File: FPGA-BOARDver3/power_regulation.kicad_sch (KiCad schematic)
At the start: 27 parts, among them Q7 DMG2305UX-13, U14 TLV62130RGTT, U15 LP5907MFX-3.3, U16 REF3012

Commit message: Power Regulation sheet 2 added
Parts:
- removed L4: 600ohm/100Mhz, symbol Device:L_Iron
- added FL2: 600Ohm/100Mhz, BLM18AG601SZ1D:BEADC1608X95N, symbol BLM18AG601SZ1D:BLM18AG601SZ1D
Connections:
- net +1V8: now also FL2.1
- net XADC1V8: now also FL2.2
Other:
- moved on the sheet: C26
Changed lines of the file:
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@@
 	)
 	(junction
+		(at 50.8 152.4)
+		(diameter 0)
+		(color 0 0 0 0)
+	)
+	(junction
 		(at 151.13 67.31)
 		(diameter 0)
@@
 	)
 	(junction
-		(at 50.8 152.4)
-		(diameter 0)
-		(color 0 0 0 0)
-	)
-	(junction
 		(at 54.61 129.54)
 		(diameter 0)
@@
 	)
 	(junction
-		(at 77.47 152.4)
+		(at 90.17 152.4)
 		(diameter 0)
 		(color 0 0 0 0)
@@
 	(wire
 		(pts
-			(xy 69.85 152.4) (xy 77.47 152.4)
-		)
-		(stroke
-			(width 0)
-			(type default)
-		)
-	)
-	(wire
-		(pts
 			(xy 116.84 39.37) (xy 119.38 39.37)
 		)
@@
 	(wire
 		(pts
-			(xy 77.47 152.4) (xy 86.36 152.4)
+			(xy 90.17 152.4) (xy 99.06 152.4)
 		)
 		(stroke
@@
 	(wire
 		(pts
+			(xy 50.8 152.4) (xy 55.88 152.4)
+		)
+		(stroke
+			(width 0)
+			(type default)
+		)
+	)
+	(wire
+		(pts
 			(xy 180.34 104.14) (xy 185.42 104.14)
 		)
@@
 	(wire
 		(pts
-			(xy 77.47 161.29) (xy 82.55 161.29)
+			(xy 90.17 161.29) (xy 95.25 161.29)
 		)
 		(stroke
@@
 	(wire
 		(pts
-			(xy 77.47 160.02) (xy 77.47 161.29)
+			(xy 90.17 160.02) (xy 90.17 161.29)
 		)
 		(stroke
@@
 	(wire
 		(pts
-			(xy 50.8 152.4) (xy 62.23 152.4)
-		)
-		(stroke
-			(width 0)
-			(type default)
-		)
-	)
-	(wire
-		(pts
 			(xy 168.91 35.56) (xy 170.18 35.56)
 		)
@@
 		)
 	)
+	(wire
+		(pts
+			(xy 83.82 152.4) (xy 90.17 152.4)
+		)
+		(stroke
+			(width 0)
+			(type default)
+		)
+	)
 	(global_label "REG5V0"
 		(shape input)
@@
 	(global_label "XADCGND"
 		(shape input)
-		(at 82.55 161.29 0)
+		(at 95.25 161.29 0)
 		(fields_autoplaced yes)
 		(effects
@@
 		)
 		(property "Intersheetrefs" "${INTERSHEET_REFS}"
-			(at 94.2438 161.29 0)
+			(at 106.9438 161.29 0)
 			(effects
 				(font
@@
 	(global_label "XADC1V8"
 		(shape input)
-		(at 86.36 152.4 0)
+		(at 99.06 152.4 0)
 		(fields_autoplaced yes)
 		(effects
@@
 		)
 		(property "Intersheetrefs" "${INTERSHEET_REFS}"
-			(at 97.6909 152.4 0)
+			(at 110.3909 152.4 0)
 			(effects
 				(font
@@
 	)
 	(symbol
-		(lib_id "Device:L_Iron")
-		(at 66.04 152.4 90)
+		(lib_id "BLM18AG601SZ1D:BLM18AG601SZ1D")
+		(at 71.12 152.4 0)
 		(unit 1)
 		(exclude_from_sim no)
@@
 		(dnp no)
 		(fields_autoplaced yes)
-		(property "Reference" "L4"
-			(at 66.04 146.05 90)
+		(property "Reference" "FL2"
+			(at 69.85 146.05 0)
 			(effects
 				(font
@@
 			)
 		)
-		(property "Value" "600ohm/100Mhz"
-			(at 66.04 148.59 90)
+		(property "Value" "600Ohm/100Mhz"
+			(at 69.85 148.59 0)
 			(effects
 				(font
@@
 			)
 		)
-		(property "Footprint" ""
-			(at 66.04 152.4 0)
+		(property "Footprint" "BLM18AG601SZ1D:BEADC1608X95N"
+			(at 71.12 152.4 0)
 			(effects
 				(font
 					(size 1.27 1.27)
 				)
+				(justify bottom)
 				(hide yes)
 			)
 		)
-		(property "Datasheet" "~"
-			(at 66.04 152.4 0)
+		(property "Datasheet" ""
+			(at 71.12 152.4 0)
 			(effects
 				(font
@@
 			)
 		)
-		(property "Description" "Inductor with iron core"
-			(at 66.04 152.4 0)
+		(property "Description" ""
+			(at 71.12 152.4 0)
 			(effects
 				(font
@@
 			)
 		)
-		(pin "1"
-		)
 		(pin "2"
 		)
+		(pin "1"
+		)
 		(instances
-			(project "FPGA-BOARDver3"
+			(project ""
 				(path "/4a327bdf-04e5-4836-9c0a-5fb801c23f64/8f1e02ad-76ee-4ea2-a502-887476bcc94b"
-					(reference "L4")
+					(reference "FL2")
 					(unit 1)
 				)
@@
 	(symbol
 		(lib_id "Device:C")
-		(at 77.47 156.21 0)
+		(at 90.17 156.21 0)
 		(unit 1)
 		(exclude_from_sim no)
@@
 		(fields_autoplaced yes)
 		(property "Reference" "C26"
-			(at 81.28 154.9399 0)
+			(at 93.98 154.9399 0)
 			(effects
 				(font
@@
 		)
 		(property "Value" "470nF"
-			(at 81.28 157.4799 0)
+			(at 93.98 157.4799 0)
 			(effects
 				(font
@@
 		)
 		(property "Footprint" ""
-			(at 78.4352 160.02 0)
+			(at 91.1352 160.02 0)
 			(effects
 				(font
@@
 		)
 		(property "Datasheet" "~"
-			(at 77.47 156.21 0)
+			(at 90.17 156.21 0)
 			(effects
 				(font
@@
 		)
 		(property "Description" "Unpolarized capacitor"
-			(at 77.47 156.21 0)
+			(at 90.17 156.21 0)
 			(effects
 				(font

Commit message: assigned footprints for power section and ddr3
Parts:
- C18, C19, C20, C21, C26, C27, C28, C29, C30, C31, C32: footprint (none) -> JLCPCB:C_0402
- Q7: footprint DMG2305UX-13:SOT91P240X110-3N -> DMG2305UX_13:SOT91P240X110-3N
- R83, R84, R85, R86, R87, R88, R89, R90, R91: footprint (none) -> JLCPCB:R_0402

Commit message: footprints added to project specific library
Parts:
- C18, C19, C20, C21, C26, C27, C28, C29, C30, C31, C32: footprint JLCPCB:C_0402 -> footprints:C_0402
- FL2: footprint BLM18AG601SZ1D:BEADC1608X95N -> footprints:BEADC1608X95N
- Q7: footprint DMG2305UX_13:SOT91P240X110-3N -> footprints:DMG2305UX_13
- R83, R84, R85, R86, R87, R88, R89, R90, R91: footprint JLCPCB:R_0402 -> footprints:R_0402
- U14: footprint TLV62130RGTT:QFN50P300X300X100-17N -> footprints:TLV62130RGTT
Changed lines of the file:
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@@
 			)
 		)
-		(property "Footprint" "JLCPCB:C_0402"
+		(property "Footprint" "footprints:C_0402"
 			(at 200.3552 43.18 0)
 			(effects
@@
 			)
 		)
-		(property "Footprint" "DMG2305UX_13:SOT91P240X110-3N"
+		(property "Footprint" "footprints:DMG2305UX_13"
 			(at 209.55 106.68 0)
 			(effects
@@
 			)
 		)
-		(property "Footprint" "JLCPCB:C_0402"
+		(property "Footprint" "footprints:C_0402"
 			(at 55.5752 129.54 0)
 			(effects
@@
 			)
 		)
-		(property "Footprint" "JLCPCB:C_0402"
+		(property "Footprint" "footprints:C_0402"
 			(at 50.4952 102.87 0)
 			(effects
@@
 			)
 		)
-		(property "Footprint" "JLCPCB:C_0402"
+		(property "Footprint" "footprints:C_0402"
 			(at 84.7852 102.87 0)
 			(effects
@@
 			)
 		)
-		(property "Footprint" "JLCPCB:R_0402"
+		(property "Footprint" "footprints:R_0402"
 			(at 243.586 122.174 90)
 			(effects
@@
 			)
 		)
-		(property "Footprint" "BLM18AG601SZ1D:BEADC1608X95N"
+		(property "Footprint" "footprints:BEADC1608X95N"
 			(at 71.12 152.4 0)
 			(effects
@@
 			)
 		)
-		(property "Footprint" "JLCPCB:C_0402"
+		(property "Footprint" "footprints:C_0402"
 			(at 51.7652 160.02 0)
 			(effects
@@
 			)
 		)
-		(property "Footprint" "TLV62130RGTT:QFN50P300X300X100-17N"
+		(property "Footprint" "footprints:TLV62130RGTT"
 			(at 149.86 50.8 0)
 			(effects
@@
 			)
 		)
-		(property "Footprint" "JLCPCB:C_0402"
+		(property "Footprint" "footprints:C_0402"
 			(at 196.5452 111.76 0)
 			(effects
@@
 			)
 		)
-		(property "Footprint" "JLCPCB:C_0402"
+		(property "Footprint" "footprints:C_0402"
 			(at 102.5652 45.72 0)
 			(effects
@@
 			)
 		)
-		(property "Footprint" "JLCPCB:R_0402"
+		(property "Footprint" "footprints:R_0402"
 			(at 94.996 32.004 90)
 			(effects
@@
 			)
 		)
-		(property "Footprint" "JLCPCB:R_0402"
+		(property "Footprint" "footprints:R_0402"
 			(at 94.996 42.164 90)
 			(effects
@@
 			)
 		)
-		(property "Footprint" "JLCPCB:R_0402"
+		(property "Footprint" "footprints:R_0402"
 			(at 188.976 53.594 90)
 			(effects
@@
 			)
 		)
-		(property "Footprint" "JLCPCB:C_0402"
+		(property "Footprint" "footprints:C_0402"
 			(at 84.7852 135.89 0)
 			(effects
@@
 			)
 		)
-		(property "Footprint" "JLCPCB:R_0402"
+		(property "Footprint" "footprints:R_0402"
 			(at 188.976 39.624 90)
 			(effects
@@
 			)
 		)
-		(property "Footprint" "JLCPCB:C_0402"
+		(property "Footprint" "footprints:C_0402"
 			(at 91.1352 160.02 0)
 			(effects
@@
 			)
 		)
-		(property "Footprint" "JLCPCB:C_0402"
+		(property "Footprint" "footprints:C_0402"
 			(at 125.4252 54.61 0)
 			(effects
@@
 			)
 		)
-		(property "Footprint" "JLCPCB:R_0402"
+		(property "Footprint" "footprints:R_0402"
 			(at 243.586 108.204 90)
 			(effects
@@
 			)
 		)
-		(property "Footprint" "JLCPCB:R_0402"
+		(property "Footprint" "footprints:R_0402"
 			(at 186.436 120.904 90)
 			(effects
@@
 			)
 		)
-		(property "Footprint" "JLCPCB:R_0402"
+		(property "Footprint" "footprints:R_0402"
 			(at 186.436 108.204 90)
 			(effects
@@
 			)
 		)
-		(property "Footprint" "JLCPCB:R_0402"
+		(property "Footprint" "footprints:R_0402"
 			(at 123.444 38.354 90)
 			(effects
@@
 			)
 		)
-		(property "Footprint" "JLCPCB:C_0402"
+		(property "Footprint" "footprints:C_0402"
 			(at 167.3352 25.4 0)
 			(effects

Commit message: spdif fpga bansks
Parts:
- removed JP1: Jumper_3_Open, symbol Jumper:Jumper_3_Open
- added J1: PJ-102AH, footprints:CUI_PJ-102AH, symbol PJ-102AH:PJ-102AH
- added J2: Conn_01x01_Pin, Connector_PinHeader_2.54mm:PinHeader_1x01_P2.54mm_Vertical, symbol Connector:Conn_01x01_Pin
- added J3: Conn_01x03_Pin, Connector_PinHeader_2.54mm:PinHeader_1x03_P2.54mm_Vertical, symbol Connector:Conn_01x03_Pin
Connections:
- net +5V: now also J3.2 (Pin_2)
- net REG5V0: now also J3.1 (Pin_1)
- net at Q7.3: now also J3.3 (Pin_3)
- net at R90.1: now also J1.1
- net GND renamed GNDREF
- net GNDREF: now also J1.2, J1.3, J2.1 (Pin_1)
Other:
- moved on the sheet: R85, R86

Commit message: update
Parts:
- J2: footprint Connector_PinHeader_2.54mm:PinHeader_1x01_P2.54mm_Vertical -> footprints:PinHeader_1x01_P2.54mm_Vertical
- J3: footprint Connector_PinHeader_2.54mm:PinHeader_1x03_P2.54mm_Vertical -> footprints:PinHeader_1x03_P2.54mm_Vertical
- U15: footprint Package_TO_SOT_SMD:SOT-23-5 -> footprints:SOT-23-5
- U16: footprint Package_TO_SOT_SMD:SOT-23 -> footprints:SOT-23
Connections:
- net VUSB: now reaches J3.3 (Pin_3), Q7.3
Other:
- moved on the sheet: C27, Q7, R83, R84

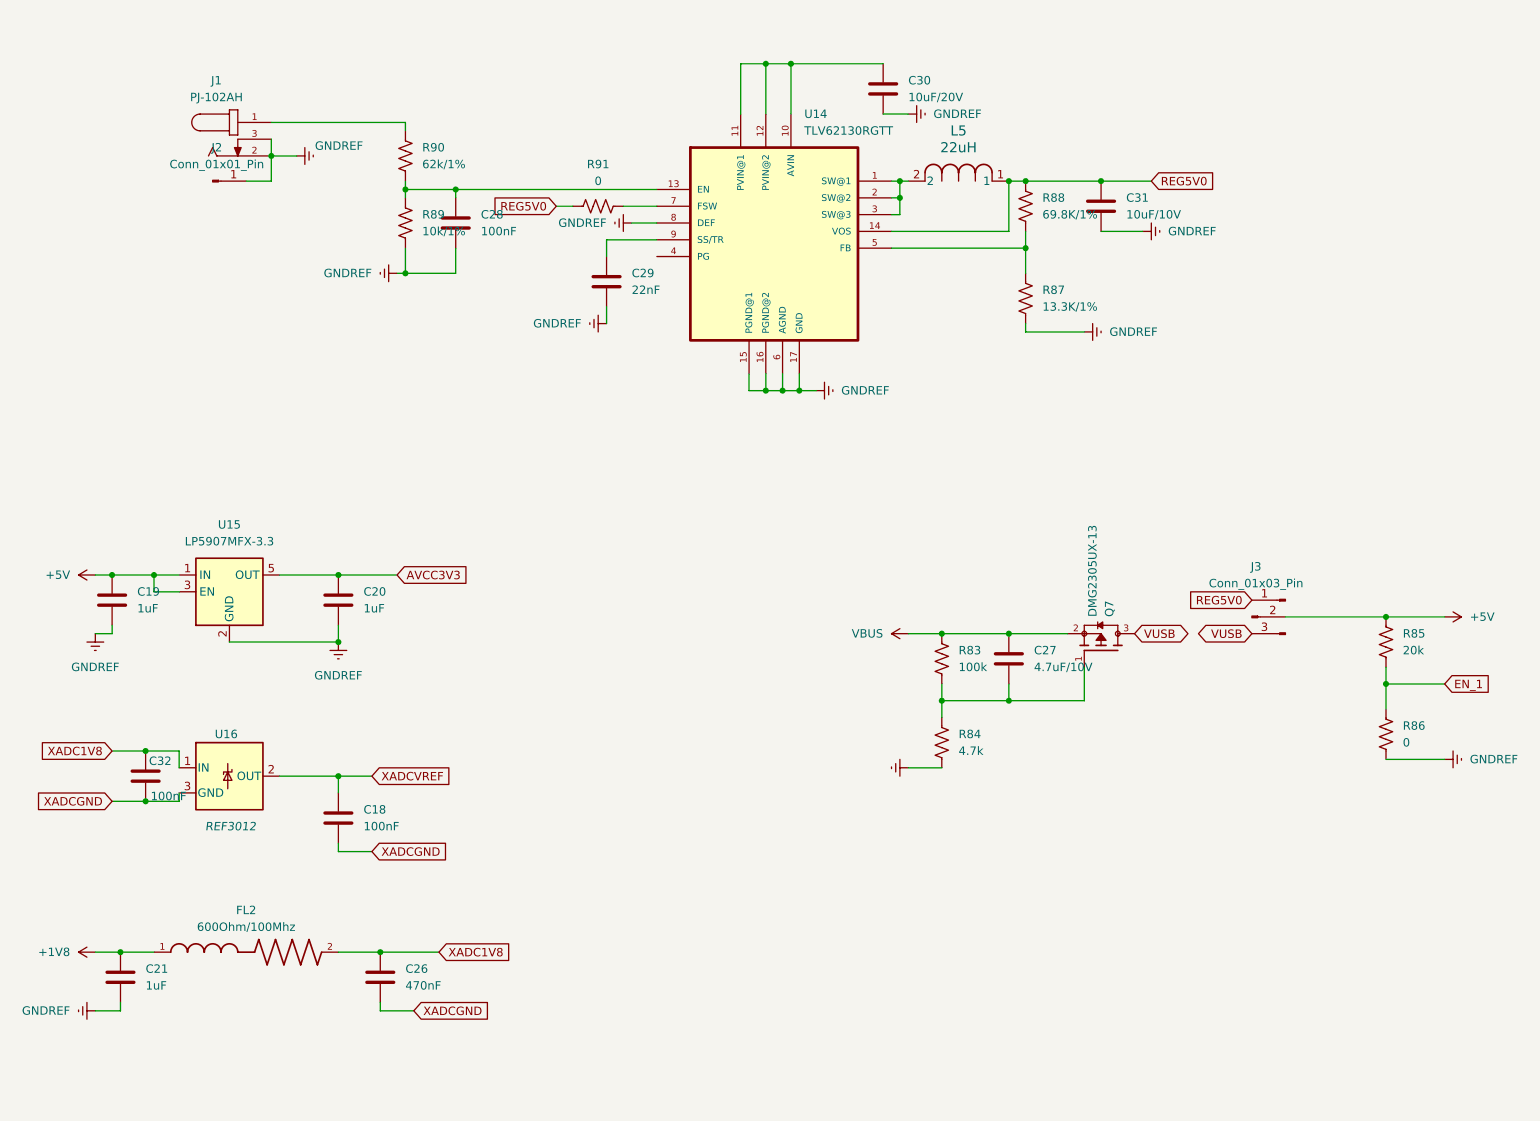
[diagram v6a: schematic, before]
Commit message: added audio out and usb
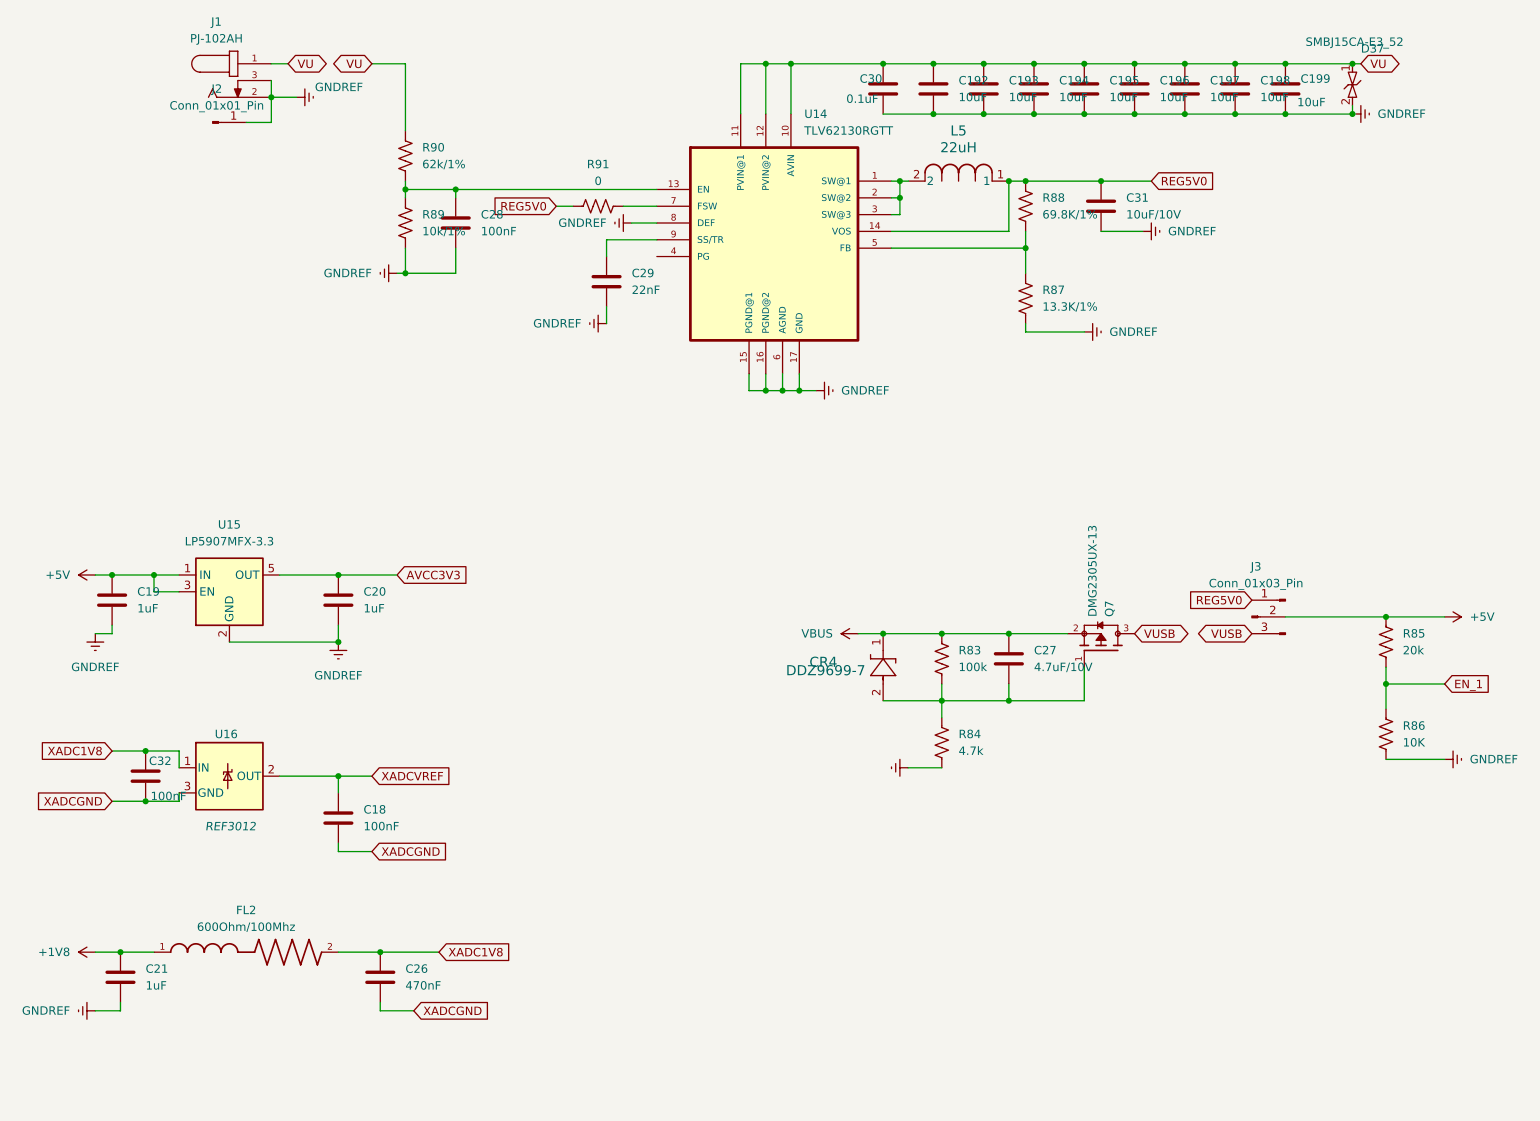
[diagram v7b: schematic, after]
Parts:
- added C192, C193, C194, C195, C196, C197, C198, C199: 10uF, footprints:C_0402, symbol Device:C
- added CR4: DDZ9699-7, footprints:ZDO_SOD123_DIO, symbol DDZ9699-7:DDZ9699-7
- added D37: SMBJ15CA-E3_52, footprints:DIOM5436X244N, symbol SMBJ15CA-E3_52:SMBJ15CA-E3_52
- C30: value 10uF/20V -> 0.1uF
- R86: value 0 -> 10K
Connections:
- net GNDREF: now also C192.2, C193.2, C194.2, C195.2, C196.2, C197.2, C198.2, C199.2, D37.2
- net VBUS: now also CR4.1
- net at C27.2, Q7.1, R83.2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: now also CR4.2
- net VU: now reaches C30.1, U14.10 (AVIN), U14.11 (PVIN@1), U14.12 (PVIN@2)
- net VU: now also J1.1, R90.1, C192.1, C193.1, C194.1, C195.1, C196.1, C197.1, C198.1, C199.1, D37.1
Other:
- moved on the sheet: J1, J2

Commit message: updated schematic and layout
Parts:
- removed L5: 22uH, footprints:IND_TAIYO_NR5040_TAY, symbol 2025-03-04_21-33-04:NR5040T2R2N
- added FL5: 600Ohm/100Mhz, footprints:BEADC1608X95N, symbol BLM18AG601SZ1D:BLM18AG601SZ1D
- added J17: Conn_01x02_Pin, footprints:PinHeader_1x02_P2.54mm_Vertical, symbol Connector:Conn_01x02_Pin
- added L3: NR5040T4R7N / 4.7uH, footprints:IND_TAIYO_NR5040_TAY, symbol NR5040T4R7N:NR5040T4R7N
- C18, C28, C30, C32: LCSC PN (none) -> c1525
- C19, C20, C21: LCSC PN (none) -> c14445
- C192, C193, C194, C195, C196, C197, C198, C199, C31: LCSC PN (none) -> c315248
- C26: LCSC PN (none) -> c92361
- C27: LCSC PN (none) -> c23733
- C29: LCSC PN (none) -> c337699
- CR4: LCSC PN (none) -> C460860
- D37: LCSC PN (none) -> C435933
- FL2, J2, J3: LCSC PN (none) -> digi/mouser
- J1: LCSC PN (none) -> C3096093
- Q7: LCSC PN (none) -> C144153
- R83: LCSC PN (none) -> C60491
- R84: LCSC PN (none) -> C105871
- R85: LCSC PN (none) -> C93942
- R86, R89: LCSC PN (none) -> C60490
- R87: LCSC PN (none) -> C274352
- R88: LCSC PN (none) -> C852893
- R90: LCSC PN (none) -> C137950
- R91: LCSC PN (none) -> C106231
- U14: LCSC PN (none) -> C122479
- U15: LCSC PN (none) -> C80670
- U16: LCSC PN (none) -> C34674
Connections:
- net +5V: now also J17.1 (Pin_1)
- net GNDREF: now also FL5.1
- net REG5V0: now also L3.1
- net XADCGND: now also FL5.2
- net at U14.1 (SW@1), U14.2 (SW@2), U14.3 (SW@3): now also L3.2
- new net PI5V: J17.2 (Pin_2)
